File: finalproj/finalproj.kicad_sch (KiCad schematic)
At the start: 8 parts

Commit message: Added lidar, stepper, dc motor conn.  more info in TODO
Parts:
- removed U?: L298N, Package_TO_SOT_THT:TO-220-15_P2.54x2.54mm_StaggerOdd_Lead4.58mm_Vertical, symbol Driver_Motor:L298N
- added J1: RPI UART, symbol Connector_Generic:Conn_01x03
- added J3: Motor_Controller_Connector, symbol finalProj:Motor_Controller_Connector
- added J4: LIDAR_Connector, symbol finalProj:LIDAR_Connector
- added J4: DC_Motor_Power_Connector, symbol finalProj:Motor_Power_Connector
- added J5: Stepper_Motor_Controller, symbol finalProj:Stepper_Motor_Controller
- added J6: Step_Motor_Power_Connector, symbol finalProj:Motor_Power_Connector
- POW1: renamed from P?; value USB_C_Plug -> RPI_POWER
- gave numbers to parts that had none: 1
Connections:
- net +12V: now also J4.1 (VIN), J6.1 (VIN)
- net +5V: now also J4.1 (POWER_IN), J5.1 (IOREF), J5.8 (NSTANDBY), J5.9 (ENB)
- net GND: now also J4.2 (POWER_EN), J4.3 (MODE), J4.6 (GND)
- new net: J4.2 (GND), J5.2 (GND), J6.2 (GND)
- new net LIDAR_SCL: J4.4 (SCL)
- new net LIDAR_SDA: J4.5 (SDA)
- new net STEP_DIR: J5.6 (DIR)
- new net STEP_PWM: J5.7 (STEP)
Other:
- note added: "Lidar"
- note added: "RPI"
- moved on the sheet: U1, U?

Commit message: main connection check readme for more info
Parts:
- removed U?: L298N, Package_TO_SOT_THT:TO-220-15_P2.54x2.54mm_StaggerOdd_Lead4.58mm_Vertical, symbol Driver_Motor:L298N
- added C? (x3): 0.1u, Capacitor_SMD:C_0805_2012Metric, symbol Device:C_Polarized_US
- added C?: 0.47u, Capacitor_SMD:C_0805_2012Metric, symbol Device:C_Polarized_US
- added J8: Programmer_Conn, symbol finalProj:Programmer_Conn
- added SW?: SW_Push, symbol Switch:SW_Push
- gave numbers to parts that had none: 4
- renumbered J4 to J7
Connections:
- net +5V: now also POW1.A4 (VBUS), POW1.A9 (VBUS), POW1.B4 (VBUS), POW1.B9 (VBUS)
- net GND: now also J1.1 (Pin_1), POW1.A1 (GND), POW1.A12 (GND), POW1.B1 (GND), POW1.B12 (GND), U1.16 (VSS), C?.2, C?.2, J8.3 (GND)
- net LIDAR_SCL: now also U1.93 (PG8)
- net LIDAR_SDA: now also U1.124 (PG9)
- net STEP_DIR: now also U1.77 (PD8)
- net STEP_PWM: now also U1.78 (PD9)
- net MotorAPWM: now reaches J3.1 (PWMA)
- net MotorAPWM: now also U1.106 (VCAP_2)
- net MotorAIn1: now reaches J3.2 (IN1)
- net MotorAIn1: now also U1.140 (PB9)
- net MotorAIn2: now reaches J3.3 (IN2)
- net MotorAIn2: now also U1.75 (PB14)
- net MotorBIn1: now reaches J3.4 (IN3)
- net MotorBIn1: now also U1.9 (PC15)
- net MotorBIn2: now reaches J3.5 (IN4)
- net MotorBIn2: now also U1.82 (PD13)
- net MotorBPWM: now reaches J3.6 (PWMB)
- net MotorBPWM: now also U1.65 (PE12)
- net RPI_UART_TX: now reaches J1.2 (Pin_2)
- net RPI_UART_TX: now also U1.22 (PF10)
- net RPI_UART_RX: now reaches J1.3 (Pin_3)
- net RPI_UART_RX: now also U1.49 (PF11)
- net at U1.23 (PH0): now also J8.2 (SWCLK)
- net at U1.30 (VDD): now also J8.1 (VDD_TARGET)
- net at U1.88 (PG3): now also J8.6 (SWO)
- new net +3V3: C?.1, C?.1
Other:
- moved on the sheet: U1

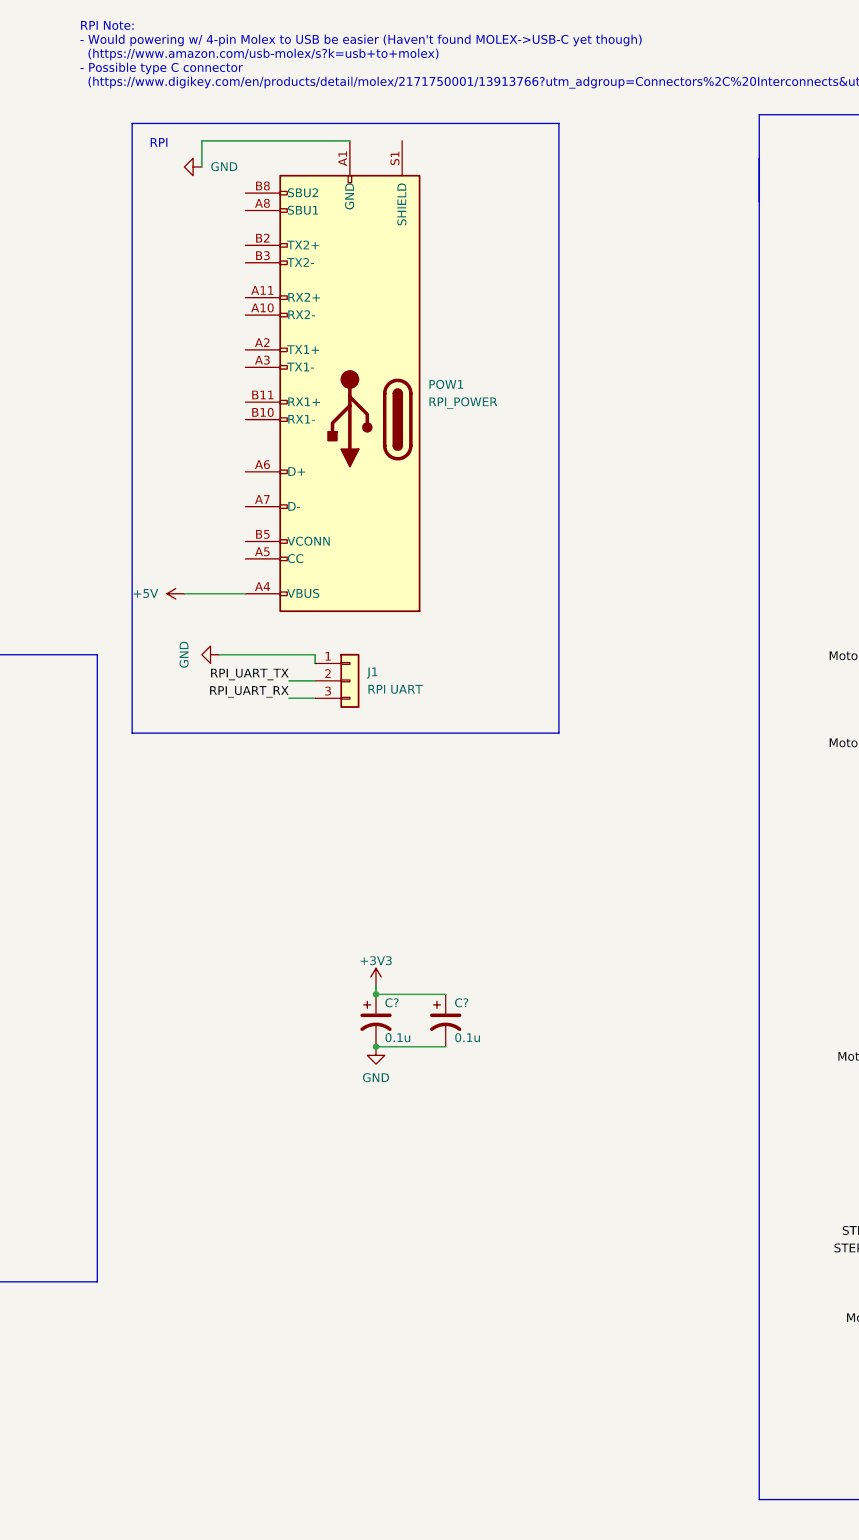
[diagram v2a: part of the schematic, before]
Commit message: added DC Motor Driver IC and peripherals
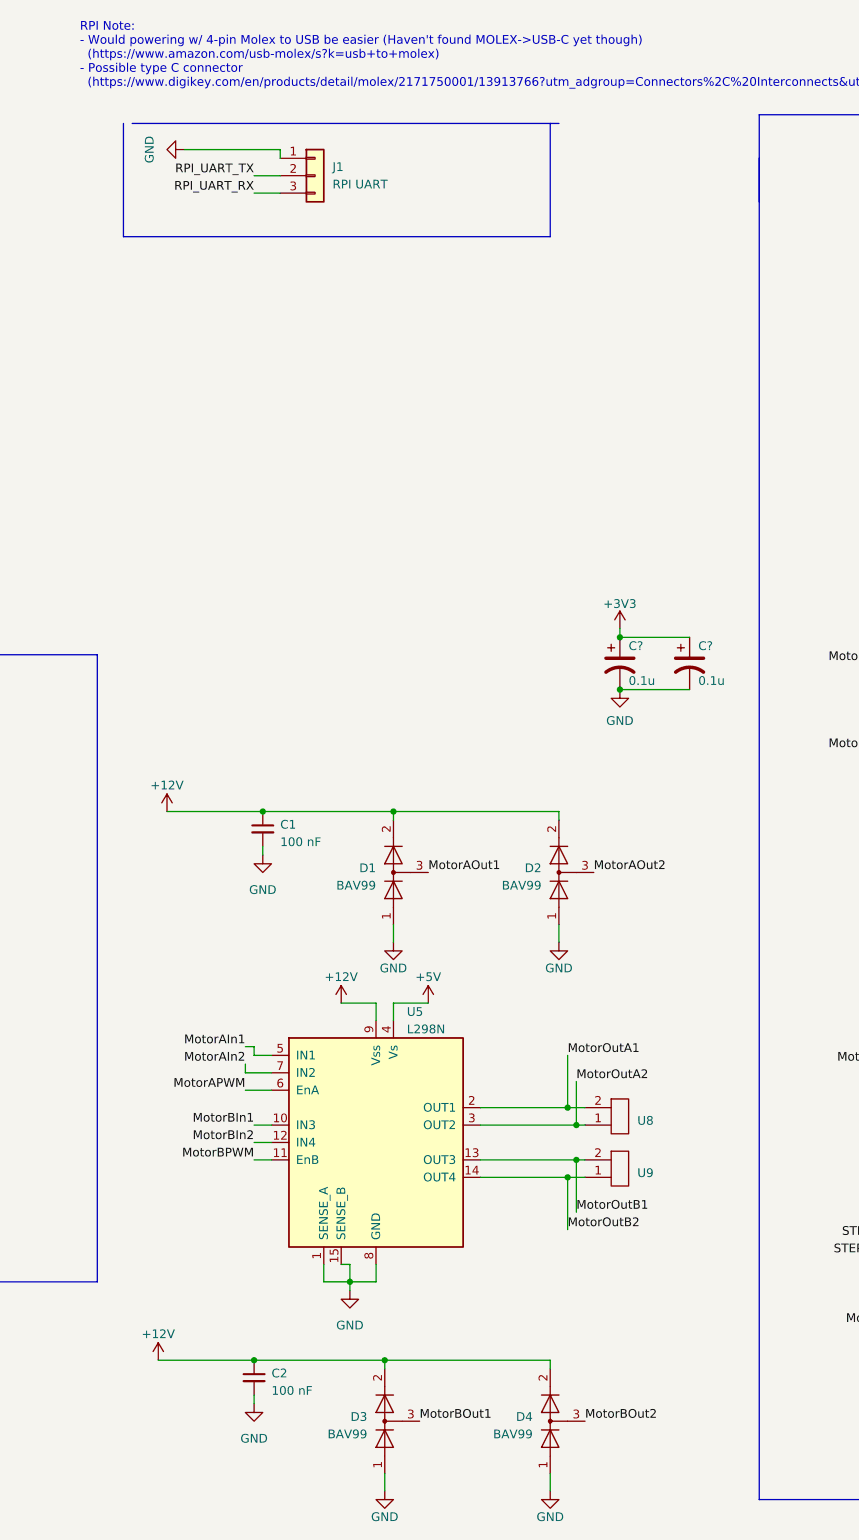
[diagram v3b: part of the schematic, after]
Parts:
- removed POW1: RPI_POWER, symbol Connector:USB_C_Plug
- added C1, C2: 100 nF, symbol Device:C_Small
- added D1, D2, D3, D4: BAV99, Package_TO_SOT_SMD:SOT-23, symbol Diode:BAV99
- added U5: L298N, Package_TO_SOT_THT:TO-220-15_P2.54x2.54mm_StaggerOdd_Lead4.58mm_Vertical, symbol Driver_Motor:L298N
- added U8, U9: ~, symbol finalproj:Motor_Output_Connector
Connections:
- net +12V: now also C1.1, C2.1, D1.2 (A), D2.2 (A), D3.2 (A), D4.2 (A), U5.9 (Vss)
- net +5V: now also U5.4 (Vs)
- net GND: now also C1.2, C2.2, D1.1 (K), D2.1 (K), D3.1 (K), D4.1 (K), U5.1 (SENSE_A), U5.15 (SENSE_B), U5.8 (GND)
- net MotorAIn1: now also U5.5 (IN1)
- net MotorAIn2: now also U5.7 (IN2)
- net MotorAPWM: now also U5.6 (EnA)
- net MotorBIn1: now also U5.10 (IN3)
- net MotorBIn2: now also U5.12 (IN4)
- net MotorBPWM: now also U5.11 (EnB)
- new net MotorAOut1: D1.3 (K)
- new net MotorAOut2: D2.3 (K)
- new net MotorBOut1: D3.3 (K)
- new net MotorBOut2: D4.3 (K)
- new net MotorOutA1: U5.2 (OUT1), U8.2 (Out-)
- new net MotorOutA2: U5.3 (OUT2), U8.1 (Out+)
- new net MotorOutB1: U5.13 (OUT3), U9.2 (Out-)
- new net MotorOutB2: U5.14 (OUT4), U9.1 (Out+)
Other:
- note removed: "RPI"
- moved on the sheet: C?, J1
